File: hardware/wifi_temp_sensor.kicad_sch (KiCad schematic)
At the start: 8 parts, among them J1 USB_B_Mini, J2 ESP8266, J3 TempSensor, J4 Prog, SW1 BootMode, U2 AZ1117-3.3

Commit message: V0.2
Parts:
- added C3, C4, C5: C_Small, Capacitor_SMD:C_1206_3216Metric, symbol Device:C_Small
- added J5: Aux_I2C, Connector_PinSocket_2.54mm:PinSocket_1x04_P2.54mm_Vertical, symbol Connector_Generic:Conn_01x04
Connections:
- net +3.3V: now also C3.1, C4.2, C5.1, J5.1 (Pin_1)
- net GND: now also C3.2, C4.1, C5.2, J5.2 (Pin_2)
- net SCL: now also J5.3 (Pin_3)
- net SDA: now also J5.4 (Pin_4)

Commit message: manual merge from esp32_msf_rcnotes
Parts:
- removed J1: USB_B_Mini, Connector_USB:USB_Micro-B_Molex-105017-0001, symbol Connector:USB_B_Mini
- removed J2: ESP8266, Connector_PinSocket_2.54mm:PinSocket_2x04_P2.54mm_Vertical, symbol Connector_Generic:Conn_02x04_Odd_Even
- removed J3: TempSensor, Connector_PinSocket_2.54mm:PinSocket_1x04_P2.54mm_Vertical, symbol Connector_Generic:Conn_01x04
- removed J4: Prog, Connector_PinHeader_2.54mm:PinHeader_1x06_P2.54mm_Vertical, symbol Connector_Generic:Conn_01x06
- removed J5: Aux_I2C, Connector_PinSocket_2.54mm:PinSocket_1x04_P2.54mm_Vertical, symbol Connector_Generic:Conn_01x04
- removed SW1: BootMode, Button_Switch_THT:SW_PUSH_6mm, symbol Switch:SW_DIP_x01
- removed U2: AZ1117-3.3, Package_TO_SOT_SMD:SOT-89-3, symbol Regulator_Linear:AZ1117-3.3
- added C10, C12: 100nF, Capacitor_SMD:C_0603_1608Metric, symbol Device:C_Small
- added C11, C6, C9: 10uF, Capacitor_SMD:C_0805_2012Metric, symbol Device:C_Small
- added C7, C8: 22pF, Capacitor_SMD:C_0603_1608Metric, symbol Device:C_Small
- added CHG1, LED1: LED_Small, LED_SMD:LED_0603_1608Metric, symbol Device:LED_Small
- added D1: D_Schottky, Diode_SMD:D_0603_1608Metric, symbol Device:D_Schottky
- added F1: Polyfuse_Small, Fuse:Fuse_0603_1608Metric, symbol Device:Polyfuse_Small
- added IC2: BQ21040DBVR, SOT95P280X145-6N, symbol BQ21040DBVR:BQ21040DBVR
- added J2: Batt_Conn, Connector_JST:JST_ACH_BM02B-ACHSS-GAN-ETF_1x02-1MP_P1.20mm_Vertical, symbol Connector:Conn_01x02_Socket
- added J3: Conn_02x03_Odd_Even, Connector_PinHeader_1.27mm:PinHeader_2x03_P1.27mm_Vertical, symbol Connector_Generic:Conn_02x03_Odd_Even
- added P1: USB_C_Plug_USB2.0, Connector_USB:USB_C_Receptacle_Palconn_UTC16-G, symbol Connector:USB_C_Plug_USB2.0
- added Q1: SSM6L09FUTE85LF, SamacSys_parts:SOT65P210X120-6N, symbol SamacSys_parts:SSM6L09FUTE85LF
- added Q2: AO3401A, Package_TO_SOT_SMD:SOT-23, symbol Transistor_FET:AO3401A
- added Q3: BSS214NW, Package_TO_SOT_SMD:SOT-323_SC-70, symbol Transistor_FET:BSS214NW
- added R1, R2: 100K, Resistor_SMD:R_0603_1608Metric, symbol Device:R_Small
- added R10, R15, R16, R3, R4: 10k, Resistor_SMD:R_0603_1608Metric, symbol Device:R_Small
- added R11: 100K, Resistor_SMD:R_0402_1005Metric, symbol Device:R_Small
- added R12, R13: 5.1K, Resistor_SMD:R_0603_1608Metric, symbol Device:R_Small
- added R14, R21: 33R, Resistor_SMD:R_0603_1608Metric, symbol Device:R_Small
- added R19: 33K, Resistor_SMD:R_0603_1608Metric, symbol Device:R_Small
- added R20, R5: 10K, Resistor_SMD:R_0603_1608Metric, symbol Device:R_Small
- added R6: 1K, Resistor_SMD:R_0603_1608Metric, symbol Device:R_Small
- added R9: R_Small, Resistor_SMD:R_0603_1608Metric, symbol Device:R_Small
- added SW1: SW_SPST, Button_Switch_SMD:SW_SPDT_CK-JS102011SAQN, symbol Switch:SW_SPST
- added SW2: SW_Push, Button_Switch_SMD:SW_SPST_B3U-3000P, symbol Switch:SW_Push
- added U1: ESP32-C3-WROOM-02, PCM_Espressif:ESP32-C3-WROOM-02, symbol PCM_Espressif:ESP32-C3-WROOM-02
- added U2: SHT4x, Sensor_Humidity:Sensirion_DFN-4_1.5x1.5mm_P0.8mm_SHT4x_NoCentralPad, symbol Sensor_Humidity:SHT4x
- added U3: WE-TVS-82400102, Package_TO_SOT_SMD:SOT-23-6, symbol Power_Protection:WE-TVS-82400102
- added U4: LD1117S33TR_SOT223, Package_TO_SOT_SMD:SOT-223-3_TabPin2, symbol Regulator_Linear:LD1117S33TR_SOT223
- C1: value 10uF -> 1uF; footprint Capacitor_SMD:C_1206_3216Metric -> Capacitor_SMD:C_0603_1608Metric
- C2: value 22uF -> 10uF; footprint Capacitor_SMD:C_1206_3216Metric -> Capacitor_SMD:C_0805_2012Metric
- C3: value C_Small -> 1uF; footprint Capacitor_SMD:C_1206_3216Metric -> Capacitor_SMD:C_0603_1608Metric
- C4: value C_Small -> 100nF; footprint Capacitor_SMD:C_1206_3216Metric -> Capacitor_SMD:C_0603_1608Metric
- C5: value C_Small -> 100nF; footprint Capacitor_SMD:C_1206_3216Metric -> Capacitor_SMD:C_0402_1005Metric
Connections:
- net +3.3V: now also C10.1, C11.1, CHG1.2 (A), J3.2 (Pin_2), LED1.2 (A), R10.1, R15.1, R16.1, R3.1, R4.1, U1.1 (3V3), U2.3 (VDD), U4.2 (VO); no longer C3.1, C4.2
- net GND: now also C4.2, C10.2, C11.2, C12.2, C6.2, C7.2, C8.2, C9.2, IC2.5 (GND), J2.1 (Pin_1), J3.6 (Pin_6), P1.A1 (GND), P1.A12 (GND), P1.B1 (GND), P1.B12 (GND), Q1.1 (SOURCE_1), Q3.2 (S), R1.2, R12.1, R13.1, R20.2, R5.2, R9.2, SW2.2, U1.19 (GND), U1.9 (GND), U2.4 (VSS), U3.2, U4.1 (GND); no longer C4.1
- net SDA: now also R4.2, U1.17 (GPIO1/ADC1_CH1/XTAL_32K_N), U2.1 (SDA)
- net +5V: no longer names the net of C1.1
- net +5V: now also D1.1 (K), Q2.2 (S), U4.3 (VI)
- new net: P1.A6 (D+), U3.1
- new net: P1.A7 (D-), U3.3
- new net: F1.1, P1.A4 (VBUS), P1.A9 (VBUS), P1.B4 (VBUS), P1.B9 (VBUS)
- new net: R15.2, U1.16 (GPIO2/ADC1_CH2)
- new net: CHG1.1 (K), R21.1
- new net: Q2.1 (G), R5.1, R6.2
- new net: P1.B5 (VCONN), R13.2
- new net: Q1.3 (DRAIN_2), R2.1
- new net: Q1.5 (GATE_2), Q1.6 (DRAIN_1), R11.2
- new net: P1.A5 (CC), R12.2
- new net: IC2.4 (ISET), R9.1
- new net: IC2.1 (TS), Q3.3 (D)
- new net: J2.2 (Pin_2), SW1.1 (A)
- new net: LED1.1 (K), R14.1
- new net CHG_ENABLE: Q3.1 (G), R16.2, U1.7 (GPIO8)
- new net D+: C7.1, U1.14 (GPIO19/USB_D+), U3.6
- new net D-: C8.1, U1.13 (GPIO18/USB_D-), U3.4
- new net EN: J3.1 (Pin_1), U1.2 (EN/CHIP_PU)
- new net IO9: J3.4 (Pin_4), U1.8 (GPIO9)
- new net RXD: J3.5 (Pin_5), U1.11 (GPIO20/U0RXD)
- new net SDC: R3.2, U1.18 (GPIO0/ADC1_CH0/XTAL_32K_P), U2.2 (SCL)
- new net TXD: J3.3 (Pin_3), U1.12 (GPIO21/U0TXD)
- new net UTIL: SW2.1, U1.10 (GPIO10)
- new net VBAT_MEAS_EN: Q1.2 (GATE_1), U1.4 (GPIO5/ADC2_CH0)
- new net V_BAT: C6.1, IC2.2 (OUT), Q1.4 (SOURCE_2), Q2.3 (D), R11.1, SW1.2 (B)
- new net V_BAT_MEAS: C4.1, R1.1, R2.2, U1.3 (GPIO4/ADC1_CH4)
- new net V_USB: C3.1, C9.1, D1.2 (A), F1.2, IC2.6 (VIN), R19.1, R6.1, U3.5
- new net V_USB_MEAS: C12.1, R19.2, R20.1, U1.15 (GPIO3/ADC1_CH3)
- new net ~{CHG}: IC2.3 (~{CHG}), R10.2, U1.6 (GPIO7)
- new net ~{CRG}: R21.2
- new net ~{LED}: R14.2, U1.5 (GPIO6)
- no-connect marks 7 -> 1
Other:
- note added: "Alt: USBLC6-2SC6"
- note added: "Has to be a P-Channel. It will turn OFF when the V_USB is present"
- note added: "I'm missing something basic. Is the 100nF cap for decoupling?"
- note added: "Is this for diag / reporting?"
- note added: "Not sure what pin 16 is for?"
- note added: "Why use a p-channel n-channel package here?"

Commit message: finished initial PCB layout
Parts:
- C10: footprint Capacitor_SMD:C_0603_1608Metric -> Capacitor_SMD:C_0805_2012Metric
- D1: footprint Diode_SMD:D_0603_1608Metric -> Diode_SMD:D_0805_2012Metric
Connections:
- net ~{CRG} is gone; now on net ~{CHG}: R21.2
- net GND: now also J2.2 (Pin_2), SW2.1; no longer J2.1 (Pin_1), SW2.2
- net SDA: now also U1.18 (GPIO0/ADC1_CH0/XTAL_32K_P); no longer U1.17 (GPIO1/ADC1_CH1/XTAL_32K_N)
- net SDC: now also U1.17 (GPIO1/ADC1_CH1/XTAL_32K_N); no longer U1.18 (GPIO0/ADC1_CH0/XTAL_32K_P)
- net UTIL: now also SW2.2; no longer SW2.1
- net V_BAT: now also SW1.1 (A); no longer SW1.2 (B)
- new net: J2.1 (Pin_1), SW1.2 (B)
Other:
- moved on the sheet: C6, J2

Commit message: corrected missing footprints
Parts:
- Q1: footprint SamacSys_parts:SOT65P210X120-6N -> SSM6N17FUTE85L:TRANS_SSM6N17FU_TE85L_F_
- U1: footprint PCM_Espressif:ESP32-C3-WROOM-02 -> Espressif:ESP32-C3-WROOM-02
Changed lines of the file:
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@@
       (effects (font (size 1.27 1.27)) (justify left))
     )
-    (property "Footprint" "PCM_Espressif:ESP32-C3-WROOM-02" (at 73.66 194.31 0)
+    (property "Footprint" "Espressif:ESP32-C3-WROOM-02" (at 73.66 194.31 0)
       (effects (font (size 1.27 1.27)) hide)
     )
@@
       (effects (font (size 1.27 1.27)))
     )
-    (property "Footprint" "SamacSys_parts:SOT65P210X120-6N" (at 91.44 -61.9 0)
+    (property "Footprint" "SSM6N17FUTE85L:TRANS_SSM6N17FU_TE85L_F_" (at 91.44 -61.9 0)
       (effects (font (size 1.27 1.27)) (justify left top) hide)
     )

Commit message: Sorting out BOM
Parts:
- C1, C12, C3, C4: Mouser Price/Stock (none) -> https://www.mouser.co.uk/ProductDetail/KYOCERA-AVX/06035C10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
- C10: Mouser Price/Stock (none) -> https://www.mouser.co.uk/ProductDetail/KYOCERA-AVX/0805ZD10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
- C11, C2, C6, C9: Mouser Price/Stock (none) -> https://www.mouser.co.uk/ProductDetail/KYOCERA-AVX/08056D10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
- C5: Mouser Price/Stock (none) -> https://www.mouser.co.uk/ProductDetail/KYOCERA-AVX/04023D10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
- C7, C8: Mouser Price/Stock (none) -> https://www.mouser.co.uk/ProductDetail/KYOCERA-AVX/06033A22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
- R1, R11, R2: value 100K -> 100k
- R12, R13: value 5.1K -> 5.1k
- R19: value 33K -> 33k
- R20, R5: value 10K -> 10k
- R6: value 1K -> 1k
- U1: Mouser Price/Stock (none) -> https://www.mouser.co.uk/ProductDetail/Espressif-Systems/ES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
- U2: Mouser Price/Stock (none) -> https://www.mouser.co.uk/ProductDetail/Sensirion/SHT40-CD1B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
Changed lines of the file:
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@@
+      (effects (font (size 1.27 1.27)) hide)
+    )
+    (property "Mouser Price/Stock" "https://www.mouser.co.uk/ProductDetail/KYOCERA-AVX/08056D106KAT4A?qs=i9jpE441ig8jHwRb12uTIA%3D%3D" (at 209.55 27.94 0)
       (effects (font (size 1.27 1.27)) hide)
     )
@@
       (effects (font (size 1.27 1.27)) (justify left))
     )
-    (property "Value" "10K" (at 100.33 83.185 0)
+    (property "Value" "10k" (at 100.33 83.185 0)
       (effects (font (size 1.27 1.27)) (justify left))
     )
@@
       (effects (font (size 1.27 1.27)) (justify left) hide)
     )
+    (property "Mouser Price/Stock" "https://www.mouser.co.uk/ProductDetail/Sensirion/SHT40-CD1B-R3?qs=ulEaXIWI0c%2FeyXO6eo5KrQ%3D%3D" (at 195.58 140.97 0)
+      (effects (font (size 1.27 1.27)) hide)
+    )
     (pin "1")
     (pin "2")
@@
       (effects (font (size 1.27 1.27)) hide)
     )
+    (property "Mouser Price/Stock" "https://www.mouser.co.uk/ProductDetail/KYOCERA-AVX/06035C104KAZ4A?qs=sGAEpiMZZMukHu%252BjC5l7YTFuG9fxNFmRImBf42zbpdM%3D" (at 228.6 93.98 0)
+      (effects (font (size 1.27 1.27)) hide)
+    )
     (pin "1")
     (pin "2")
@@
     )
     (property "Datasheet" "https://www.espressif.com/sites/default/files/documentation/esp32-c3-wroom-02_datasheet_en.pdf" (at 71.12 196.85 0)
+      (effects (font (size 1.27 1.27)) hide)
+    )
+    (property "Mouser Price/Stock" "https://www.mouser.co.uk/ProductDetail/Espressif-Systems/ESP32-C3-WROOM-02-H4?qs=sGAEpiMZZMsjLMBIknjmknKJE5m7ZCsm2cYf5nU5BebEZP24kwUjVg%3D%3D" (at 73.66 163.83 0)
       (effects (font (size 1.27 1.27)) hide)
     )
@@
       (effects (font (size 1.27 1.27)) hide)
     )
+    (property "Mouser Price/Stock" "https://www.mouser.co.uk/ProductDetail/KYOCERA-AVX/08056D106KAT4A?qs=i9jpE441ig8jHwRb12uTIA%3D%3D" (at 44.45 72.39 0)
+      (effects (font (size 1.27 1.27)) hide)
+    )
     (pin "1")
     (pin "2")
@@
       (effects (font (size 1.27 1.27)) (justify left))
     )
-    (property "Value" "33K" (at 100.33 70.485 0)
+    (property "Value" "33k" (at 100.33 70.485 0)
       (effects (font (size 1.27 1.27)) (justify left))
     )
@@
       (effects (font (size 1.27 1.27)))
     )
-    (property "Value" "1K" (at 208.28 93.98 90)
+    (property "Value" "1k" (at 208.28 93.98 90)
       (effects (font (size 1.27 1.27)))
     )
@@
       (effects (font (size 1.27 1.27)) (justify left))
     )
-    (property "Value" "10K" (at 217.17 102.87 0)
+    (property "Value" "10k" (at 217.17 102.87 0)
       (effects (font (size 1.27 1.27)) (justify left))
     )
@@
       (effects (font (size 1.27 1.27)))
     )
-    (property "Value" "5.1K" (at 242.57 30.48 90)
+    (property "Value" "5.1k" (at 242.57 30.48 90)
       (effects (font (size 1.27 1.27)))
     )
@@
       (effects (font (size 1.27 1.27)) hide)
     )
+    (property "Mouser Price/Stock" "https://www.mouser.co.uk/ProductDetail/KYOCERA-AVX/06035C104KAZ4A?qs=sGAEpiMZZMukHu%252BjC5l7YTFuG9fxNFmRImBf42zbpdM%3D" (at 87.63 68.58 0)
+      (effects (font (size 1.27 1.27)) hide)
+    )
     (pin "1")
     (pin "2")
@@
       (effects (font (size 1.27 1.27)) hide)
     )
+    (property "Mouser Price/Stock" "https://www.mouser.co.uk/ProductDetail/KYOCERA-AVX/06033A220JAT2A?qs=9MLDsNTH4mOP2O4%2FmNvAAA%3D%3D" (at 207.01 48.26 0)
+      (effects (font (size 1.27 1.27)) hide)
+    )
     (pin "1")
     (pin "2")
@@
       (effects (font (size 1.27 1.27)) hide)
     )
+    (property "Mouser Price/Stock" "https://www.mouser.co.uk/ProductDetail/KYOCERA-AVX/04023D104KAT2A?qs=QxF4U1u29WAufkrwnFhHEQ%3D%3D" (at 205.74 140.97 0)
+      (effects (font (size 1.27 1.27)) hide)
+    )
     (pin "1")
     (pin "2")
@@
     )
     (property "Datasheet" "~" (at 54.61 134.62 0)
+      (effects (font (size 1.27 1.27)) hide)
+    )
+    (property "Mouser Price/Stock" "https://www.mouser.co.uk/ProductDetail/KYOCERA-AVX/08056D106KAT4A?qs=i9jpE441ig8jHwRb12uTIA%3D%3D" (at 54.61 134.62 0)
       (effects (font (size 1.27 1.27)) hide)
     )
@@
       (effects (font (size 1.27 1.27)) (justify left))
     )
-    (property "Value" "100K" (at 147.32 37.465 0)
+    (property "Value" "100k" (at 147.32 37.465 0)
       (effects (font (size 1.27 1.27)) (justify left))
     )
@@
       (effects (font (size 1.27 1.27)) (justify left))
     )
-    (property "Value" "100K" (at 80.01 35.56 0)
+    (property "Value" "100k" (at 80.01 35.56 0)
       (effects (font (size 1.27 1.27)) (justify left))
     )
@@
       (effects (font (size 1.27 1.27)) hide)
     )
+    (property "Mouser Price/Stock" "https://www.mouser.co.uk/ProductDetail/KYOCERA-AVX/06033A220JAT2A?qs=9MLDsNTH4mOP2O4%2FmNvAAA%3D%3D" (at 215.9 48.26 0)
+      (effects (font (size 1.27 1.27)) hide)
+    )
     (pin "1")
     (pin "2")
@@
       (effects (font (size 1.27 1.27)) hide)
     )
+    (property "Mouser Price/Stock" "https://www.mouser.co.uk/ProductDetail/KYOCERA-AVX/08056D106KAT4A?qs=i9jpE441ig8jHwRb12uTIA%3D%3D" (at 252.73 93.98 0)
+      (effects (font (size 1.27 1.27)) hide)
+    )
     (pin "1")
     (pin "2")
@@
       (effects (font (size 1.27 1.27)) hide)
     )
+    (property "Mouser Price/Stock" "https://www.mouser.co.uk/ProductDetail/KYOCERA-AVX/06035C104KAZ4A?qs=NI4NqA541gtiVdo7Hwl8%252BQ%3D%3D" (at 110.49 81.28 0)
+      (effects (font (size 1.27 1.27)) hide)
+    )
     (pin "1")
     (pin "2")
@@
       (effects (font (size 1.27 1.27)))
     )
-    (property "Value" "5.1K" (at 242.57 27.94 90)
+    (property "Value" "5.1k" (at 242.57 27.94 90)
       (effects (font (size 1.27 1.27)))
     )
@@
       (effects (font (size 1.27 1.27)) hide)
     )
+    (property "Mouser Price/Stock" "https://www.mouser.co.uk/ProductDetail/KYOCERA-AVX/0805ZD104KAT2A?qs=qVfB0%2FDaMDZM7gCosjcOHQ%3D%3D" (at 63.5 134.62 0)
+      (effects (font (size 1.27 1.27)) hide)
+    )
     (pin "1")
     (pin "2")
@@
     )
     (property "Datasheet" "~" (at 157.48 45.72 0)
+      (effects (font (size 1.27 1.27)) hide)
+    )
+    (property "Mouser Price/Stock" "https://www.mouser.co.uk/ProductDetail/KYOCERA-AVX/06035C104KAZ4A?qs=NI4NqA541gtiVdo7Hwl8%252BQ%3D%3D" (at 157.48 45.72 0)
       (effects (font (size 1.27 1.27)) hide)
     )
@@
       (effects (font (size 1.27 1.27)) (justify left))
     )
-    (property "Value" "100K" (at 147.32 47.625 0)
-      (effects (font (size 1.27 1.27)) (justify left))
-    )
+    (property "Value" "100k" (at 147.32 47.625 0)
+      (effects (font (size 1.27 1.27)) (justify left))
+    )

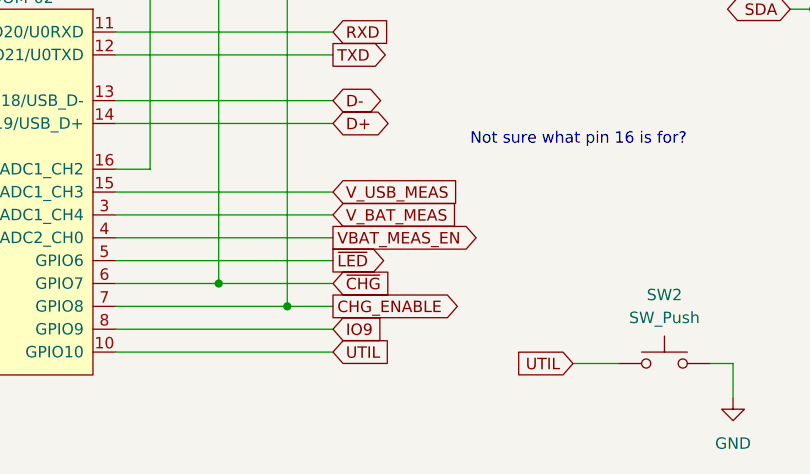
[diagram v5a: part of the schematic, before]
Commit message: re-routed util switch to GPIO4 for deep sleep wakeup, re-routed USB to get the differental impedance to nearer to 90ohms
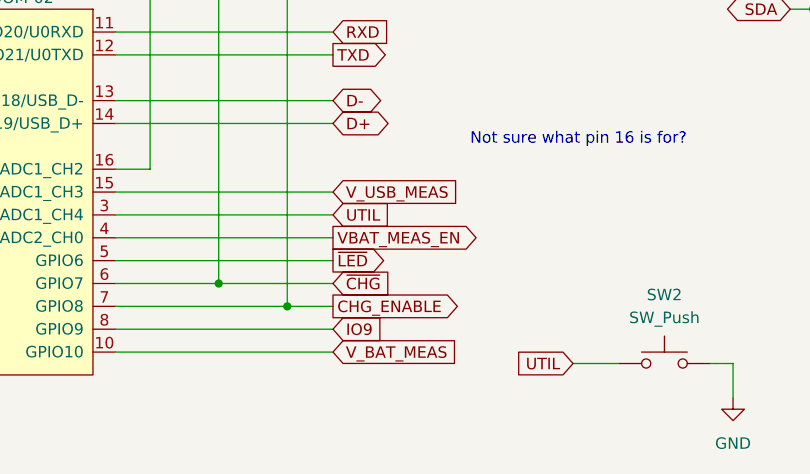
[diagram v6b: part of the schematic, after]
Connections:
- net UTIL: now also U1.3 (GPIO4/ADC1_CH4); no longer U1.10 (GPIO10)
- net V_BAT_MEAS: now also U1.10 (GPIO10); no longer U1.3 (GPIO4/ADC1_CH4)
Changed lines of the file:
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@@
+    (stroke (width 0) (type default))
+  )
+  (wire (pts (xy 101.6 166.37) (xy 125.73 166.37))
     (stroke (width 0) (type default))
   )
@@
     (stroke (width 0) (type default))
   )
+  (wire (pts (xy 101.6 181.61) (xy 125.73 181.61))
+    (stroke (width 0) (type default))
+  )
   (wire (pts (xy 196.85 87.63) (xy 209.55 87.63))
     (stroke (width 0) (type default))
@@
     (stroke (width 0) (type default))
   )
-  (wire (pts (xy 101.6 181.61) (xy 125.73 181.61))
-    (stroke (width 0) (type default))
-  )
   (wire (pts (xy 139.7 91.44) (xy 139.7 97.79))
     (stroke (width 0) (type default))
@@
   )
   (wire (pts (xy 228.6 87.63) (xy 228.6 91.44))
-    (stroke (width 0) (type default))
-  )
-  (wire (pts (xy 101.6 166.37) (xy 125.73 166.37))
     (stroke (width 0) (type default))
   )
@@
     )
   )
-  (global_label "V_BAT_MEAS" (shape input) (at 125.73 166.37 0) (fields_autoplaced)
-    (effects (font (size 1.27 1.27)) (justify left))
-    (property "Intersheetrefs" "${INTERSHEET_REFS}" (at 139.9637 166.37 0)
+  (global_label "V_BAT_MEAS" (shape input) (at 125.73 181.61 0) (fields_autoplaced)
+    (effects (font (size 1.27 1.27)) (justify left))
+    (property "Intersheetrefs" "${INTERSHEET_REFS}" (at 139.9637 181.61 0)
       (effects (font (size 1.27 1.27)) (justify left) hide)
     )
@@
     )
   )
-  (global_label "UTIL" (shape input) (at 125.73 181.61 0) (fields_autoplaced)
-    (effects (font (size 1.27 1.27)) (justify left))
-    (property "Intersheetrefs" "${INTERSHEET_REFS}" (at 132.6462 181.61 0)
-      (effects (font (size 1.27 1.27)) (justify left) hide)
-    )
+  (global_label "UTIL" (shape input) (at 125.73 166.37 0) (fields_autoplaced)
+    (effects (font (size 1.27 1.27)) (justify left))
+    (property "Intersheetrefs" "${INTERSHEET_REFS}" (at 132.6462 166.37 0)
+      (effects (font (size 1.27 1.27)) (justify left) hide)
+    )
